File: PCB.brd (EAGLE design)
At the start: 45.3 x 36 mm, 27 parts, among them U1 MSP430G2553_PW_20, U2 DRV8833_PWP_16, U3 DRV8833_PWP_16

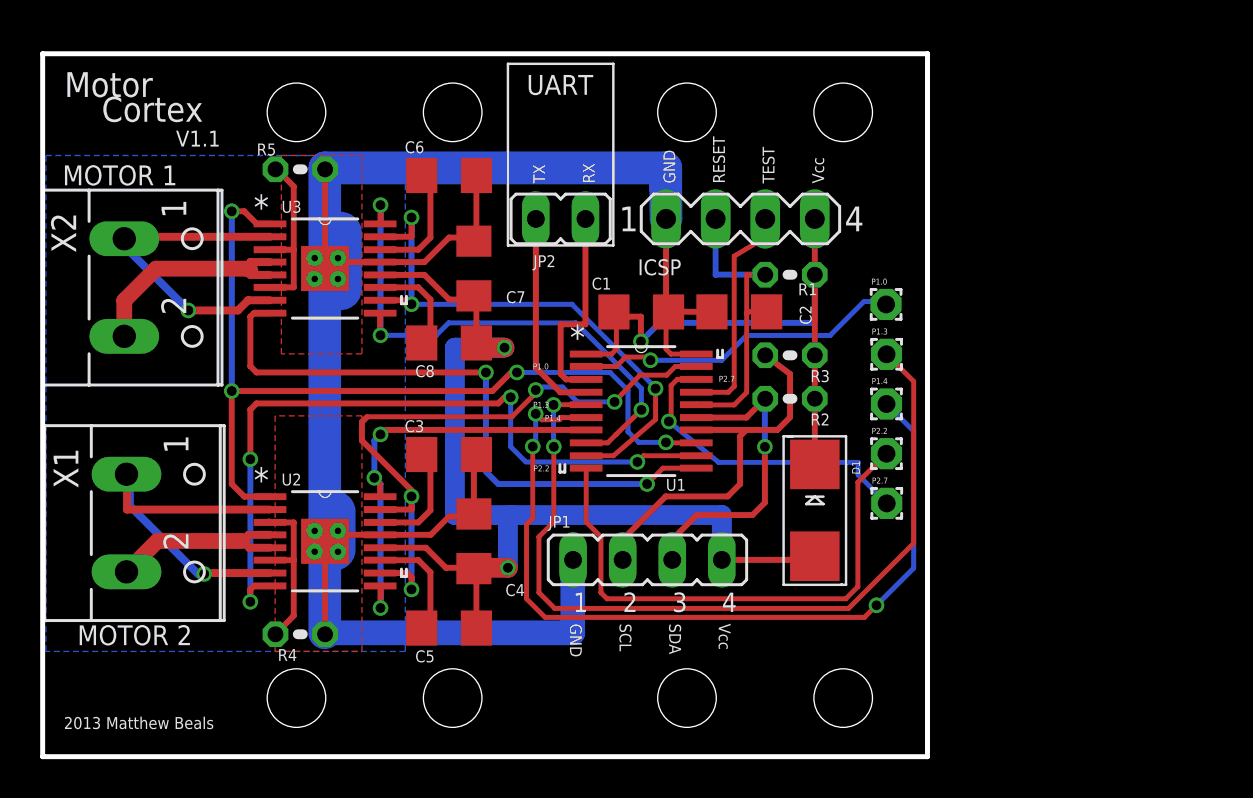
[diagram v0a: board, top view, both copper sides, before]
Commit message: added power board and gitignore
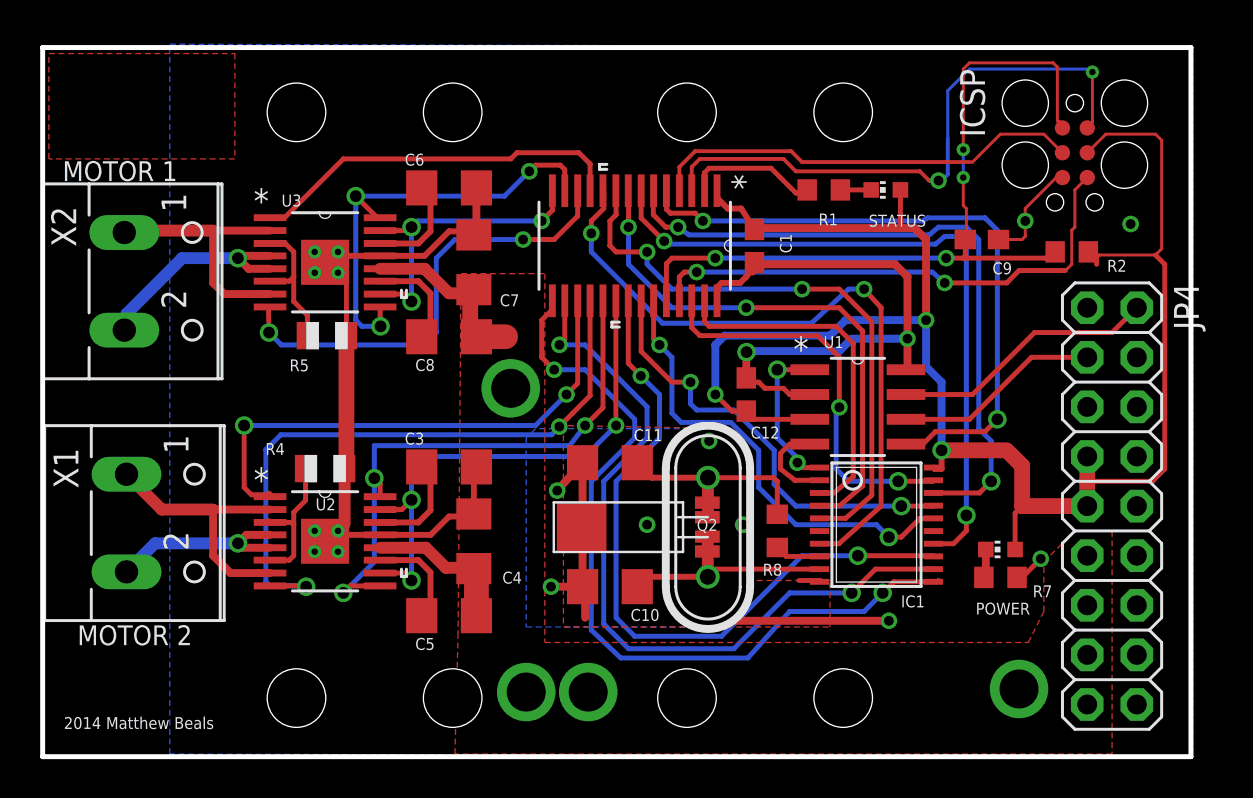
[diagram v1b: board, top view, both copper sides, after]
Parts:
- removed C2: 1 nF, adafruit:C1206
- removed D1: (no value), adafruit:SMADIODE
- removed JP1: (no value), jumper:JP4
- removed JP2: (no value), jumper:JP1
- removed P1.0, P1.3, P1.4, P2.2, P2.7: (no value), wirepad:1,6/0,9
- removed R3: 200k, adafruit:0204V
- added C10, C11: 23p, adafruit:C1206
- added C12: (no value), adafruit:C0603
- added C9: 2.2n, adafruit:C0603
- added IC1: MCP2515-E/ST, mcp2515:TSSOP20
- added JP4: (no value), adafruit:2X09-BIG
- added POWER, STATUS: (no value), adafruit:CHIP-LED0603
- added Q2: QUARZ5, sMSP430:QUARZ5
- added R7, R8: (no value), adafruit:R0603
- added U5: MSP430G2553_PW_28, TexasInstruments:PW28
- C1: device adafruit:C1206 -> adafruit:C0603
- ICSP: value (none) -> 6-PIN-ICSPTAGCONNECT-HOLES; device con-lstb:MA04-1 -> LaunchFET:TAGCONNECT-HOLES
- R1: device adafruit:0204V -> adafruit:R0603
- R2: value 200k -> 47k; device adafruit:0204V -> adafruit:R0603
- R4, R5: device adafruit:0204V -> adafruit:R0805
- U1: value MSP430G2553_PW_20 -> SN65HVD235_D_8; device TI:PW20 -> TexasInstruments:D8
- moved ICSP 17.5 mm to (62.9, 74.9), turned to 270 degrees
- moved R2 16.3 mm to (62.7, 69.8)
- moved U1 11.1 mm to (51.8, 61.9)
- moved R5 8.63 mm to (24.6, 65.6)
- moved R4 8.58 mm to (24.5, 58.8)
- moved C1 6.71 mm to (46.5, 70.2), turned to 270 degrees
- moved R1 4.67 mm to (50.0, 73.0), turned to 180 degrees
- moved C6 0.64 mm to (30.8, 73.1)
- moved C3 0.63 mm to (30.8, 58.8)
- moved C5 0.63 mm to (30.8, 51.2)
- moved X2 0.32 mm to (15.5, 68.3)
- moved C7 0.32 mm to (32.1, 69.3)
- moved C8 0.32 mm to (30.8, 65.5)
- moved U3 0.32 mm to (24.5, 69.3)
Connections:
- removed net +3V3MOTOR: C4.2, C5.1, C7.2, C8.1, D1.A, JP1.4, U2.12, U3.12
- removed net NRESET: U1.13, U2.1, U3.1
- removed net P1.0: P1.0.1, U1.2
- removed net P1.3: P1.3.1, U1.5
- removed net P1.4: P1.4.1, U1.6
- removed net P2.2: P2.2.1, U1.10
- removed net P2.7: P2.7.1, U1.18
- removed net SCL: JP1.2, R3.1, U1.14
- removed net SDA: JP1.3, R2.1, U1.15
- new net AUTO_BAUD: U1.5, U5.5
- new net CAN_H: JP4.2, U1.7
- new net CAN_L: JP4.3, U1.6
- new net CAN_RESET: IC1.19, U5.26
- new net CLK: IC1.14, U5.7
- new net EXT_XIN: IC1.3, U5.27
- new net LED0: R1.2, U5.2
- new net MISO: IC1.17, U5.22
- new net MOSI: IC1.16, U5.23
- new net N$2: R1.1, STATUS.C
- new net N$5: POWER.C, R7.1
- new net N1RESET: U2.1, U5.17
- new net N2RESET: U3.1, U5.11
- new net RX0BF: IC1.12, U5.16
- new net RX1BF: IC1.11, U5.15
- new net RXINT: IC1.13, U5.21
- new net RX_CAN: IC1.2, U1.4
- new net STE: IC1.18, U5.6
- new net TX0RTS: IC1.4, U5.8
- new net TX1RTS: IC1.5, U5.9
- new net TX2RTS: IC1.7, U5.10
- new net TX_CAN: IC1.1, U1.1
- new net VBUS: C4.2, C5.1, C7.2, C8.1, JP4.11, JP4.13, JP4.15, JP4.17, U2.12, U3.12
- new net XIN: C10.1, IC1.9, Q2.2
- new net XOUT: IC1.8, R8.1
- new net XOUT_C: C11.1, Q2.1, R8.2
- net +3V3: now also C12.1, IC1.20, JP4.7, JP4.9, POWER.A, STATUS.A, U1.3, U5.1; no longer D1.C, R1.2, R3.2, U1.1
- net GND: now also C10.2, C11.2, C12.2, C9.2, IC1.10, ICSP.5, JP4.1, JP4.12, JP4.14, JP4.16, JP4.18, JP4.4, JP4.5, JP4.6, Q2.GND@0, R7.2, U1.2, U1.8, U5.28; no longer C2.2, ICSP.1, JP1.1, U1.20
- net N1ERROR: now also U5.18; no longer U1.12
- net N1IN1: now also U5.19; no longer U1.7
- net N1IN2: now also U5.20; no longer U1.19
- net N2ERROR: now also U5.12; no longer U1.11
- net N2IN1: now also U5.13; no longer U1.8
- net N2IN2: now also U5.14; no longer U1.9
- net RST: now also C9.1, ICSP.1, R2.1, U5.24; no longer C2.1, ICSP.2, R1.1, U1.16
- net TEST: now also ICSP.6, U5.25; no longer ICSP.3, U1.17
- net UART_RX: now also ICSP.2, U5.3; no longer JP2.1, U1.3
- net UART_TX: now also ICSP.3, U5.4; no longer JP2.2, U1.4
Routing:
- net +3V3: track 30.5 -> 90.5 mm, vias 1 -> 3
- net +3V3MOTOR: track 55.5 -> 0.00 mm, vias 2 -> 0
- net NRESET: track 45.4 -> 0.00 mm, vias 4 -> 0
- net P1.3: track 42.8 -> 0.00 mm, vias 2 -> 0
- net P1.4: track 42.7 -> 0.00 mm, vias 3 -> 0
- net RX1BF: track 0.00 -> 41.0 mm, vias 0 -> 2
- net RX0BF: track 0.00 -> 39.3 mm, vias 0 -> 2
- net RXINT: track 0.00 -> 36.2 mm, vias 0 -> 2
- net CLK: track 0.00 -> 35.5 mm, vias 0 -> 2
- net TX2RTS: track 0.00 -> 34.9 mm, vias 0 -> 2
- net STE: track 0.00 -> 34.6 mm, vias 0 -> 2
- net AUTO_BAUD: track 0.00 -> 33.3 mm, vias 0 -> 2
- net TX1RTS: track 0.00 -> 30.4 mm, vias 0 -> 2
- net TX0RTS: track 0.00 -> 27.7 mm, vias 0 -> 2
- net P2.2: track 27.7 -> 0.00 mm
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- added copper zone on layer 1, net N$1
- added copper zone on layer 1, net VBUS
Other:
- board size 45.3 x 36 mm -> 58.8 x 36.3 mm
- board text added: "2014 Matthew Beals"
- board text removed: "2013 Matthew Beals"
- board text removed: "GND"
- board text removed: "P1.0"
- board text removed: "P1.3"
- board text removed: "P1.4"
- board text removed: "P2.2"
- board text removed: "P2.7"
- board text removed: "RESET"
- board text removed: "RX"
- board text removed: "SCL"
- board text removed: "SDA"
- board text removed: "TEST"
- board text removed: "TX"
- board text removed: "UART"
- board text removed: "Vcc"

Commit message: major topology changes
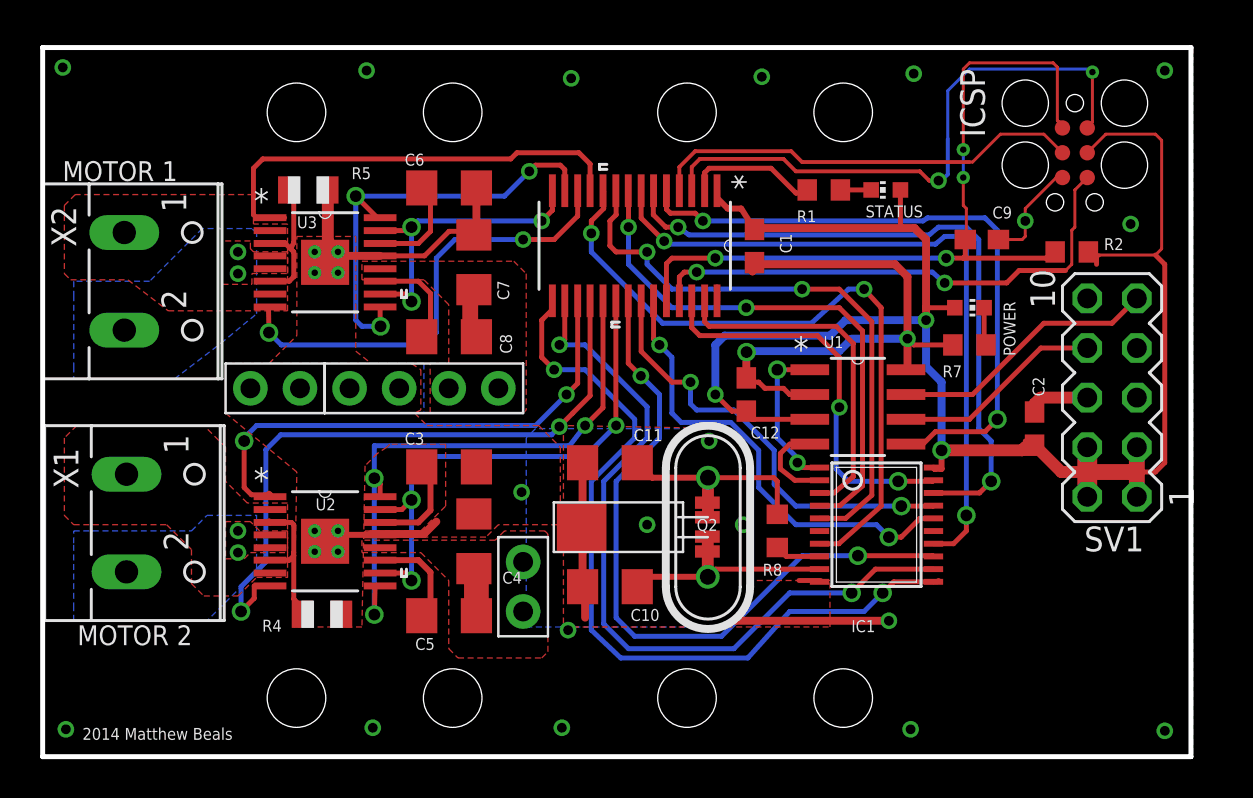
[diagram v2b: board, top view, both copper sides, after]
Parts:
- removed JP4: (no value), adafruit:2X09-BIG
- added C2: (no value), adafruit:C0603
- added SV1: (no value), con-lstb:MA05-2
- added U$2: 1X4_HEADER, connectors:1X4-.1HEADER
- added U$3, U$4: 1X2_HEADER, connectors:1X2-.1HEADER
- moved POWER 12.5 mm to (57.5, 67.0), turned to 270 degrees
- moved R7 12.0 mm to (57.5, 65.1), turned to 180 degrees
- moved R5 7.52 mm to (23.6, 73.0)
- moved R4 7.46 mm to (24.3, 51.3)
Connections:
- removed net VBUS: C4.2, C5.1, C7.2, C8.1, JP4.11, JP4.13, JP4.15, JP4.17, U2.12, U3.12
- new net VBUS-M1: C7.2, C8.1, U$2.3, U$2.4, U3.12
- new net VBUS-M2: C4.2, C5.1, U$4.1, U$4.2, U2.12
- net +3V3: now also C2.1, SV1.1, SV1.2, SV1.3, SV1.4; no longer JP4.7, JP4.9
- net CAN_H: now also SV1.9; no longer JP4.2
- net CAN_L: now also SV1.8; no longer JP4.3
- net GND: now also C2.2, SV1.10, SV1.5, SV1.6, SV1.7, U$2.1, U$2.2, U$3.1, U$3.2; no longer JP4.1, JP4.12, JP4.14, JP4.16, JP4.18, JP4.4, JP4.5, JP4.6
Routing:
- net VBUS: track 18.1 -> 0.00 mm, vias 4 -> 0
- net GND: track 93.6 -> 79.3 mm, vias 11 -> 21
- net N1OUT1: track 13.7 -> 0.00 mm
- net N2OUT1: track 13.3 -> 0.14 mm
- net N2OUT2: track 11.3 -> 0.00 mm, vias 1 -> 2
- net N1OUT2: track 9.87 -> 0.00 mm, vias 1 -> 2
- net N2RESET: track 19.4 -> 23.2 mm
- net VBUS-M2: track 0.00 -> 3.60 mm
- net VBUS-M1: track 0.00 -> 2.62 mm
- added copper zone on layer 1, net N1OUT1
- added copper zone on layer 1, net N1OUT2
- added copper zone on layer 16, net N1OUT2
- added copper zone on layer 1, net N2OUT1
- added copper zone on layer 1, net N2OUT2
- added copper zone on layer 16, net N2OUT2
- added copper zone on layer 1, net VBUS-M1
- added copper zone on layer 1, net VBUS-M2
- removed copper zone on layer 1, net N$1
- removed copper zone on layer 1, net VBUS
